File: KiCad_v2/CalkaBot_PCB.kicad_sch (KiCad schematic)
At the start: 38 parts, among them J1 Conn_01x03_Pin, J2 Conn_01x03_Pin, J3 Conn_01x03_Pin, J4 Conn_01x02_Pin, J5 MOTOR3, J6 StartModule, M1 Motor_Right, M2 Motor_Left, Q1 KTIR0711S, Q2 KTIR0711S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

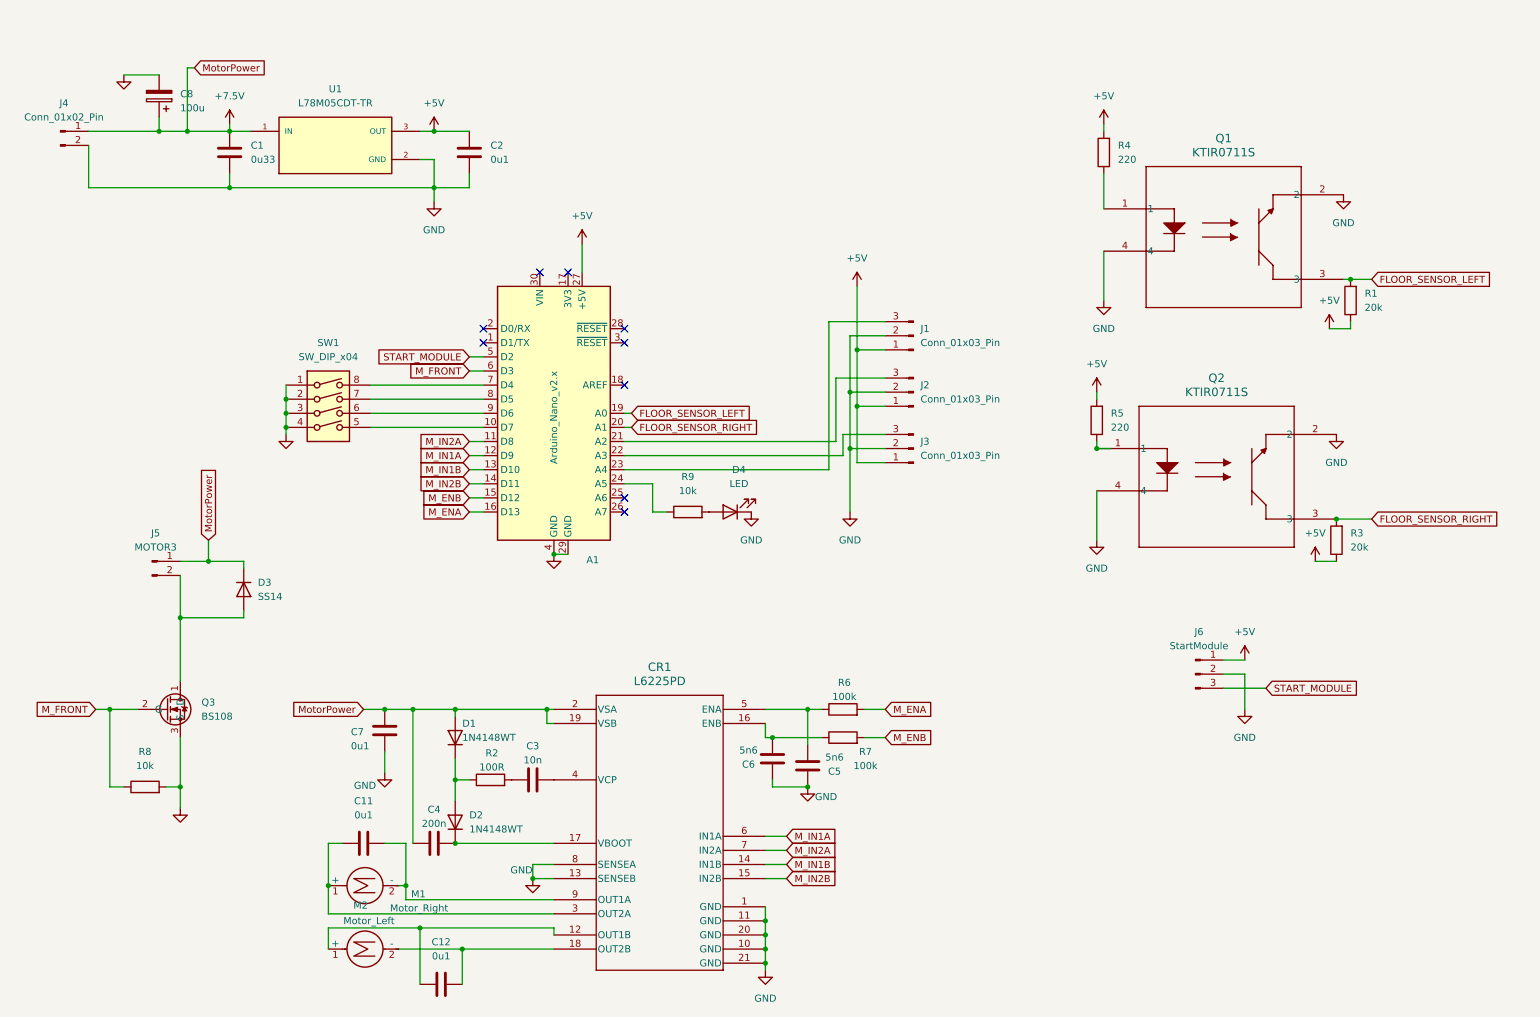
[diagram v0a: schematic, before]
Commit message: Druga płytka działa i jeździ
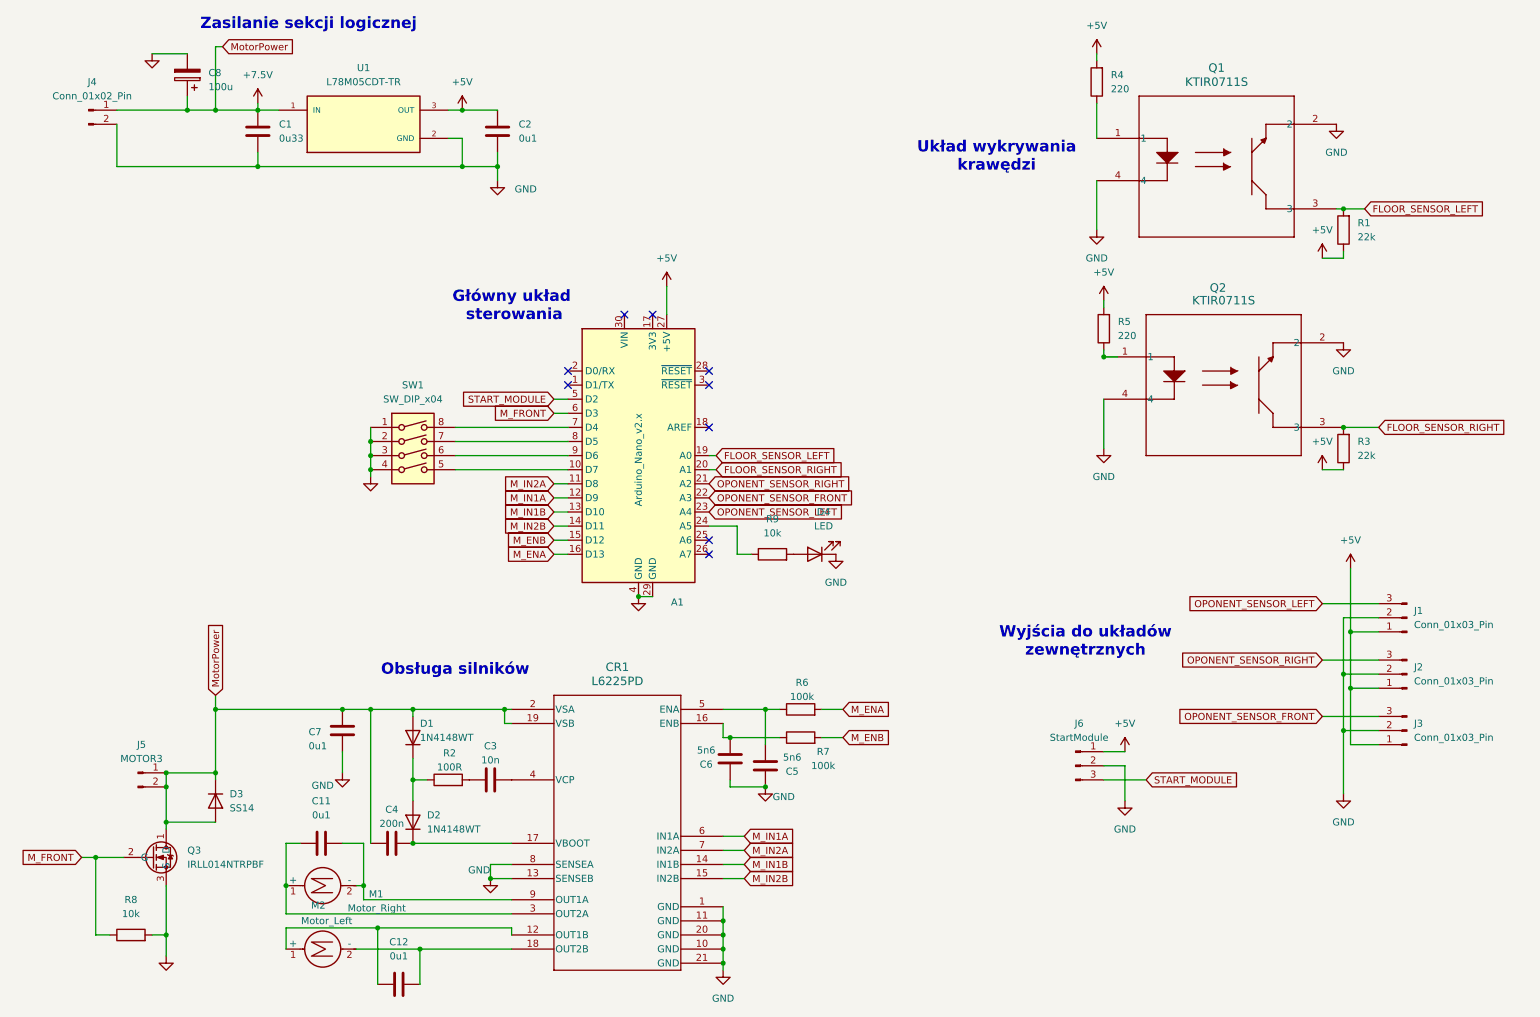
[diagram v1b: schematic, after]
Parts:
- Q3: value BS108 -> IRLL014NTRPBF
- R1, R3: value 20k -> 22k
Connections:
- net +7.5V: now also D3.2 (A), J5.2 (Pin_2), Q3.1 (D)
- net OPONENT_SENSOR_LEFT: now reaches A1.23 (A4), J1.3 (Pin_3)
- net OPONENT_SENSOR_RIGHT: now reaches A1.21 (A2), J2.3 (Pin_3)
- net OPONENT_SENSOR_FRONT: now reaches A1.22 (A3), J3.3 (Pin_3)
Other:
- note added: "Główny układ sterowania"
- note added: "Obsługa silników"
- note added: "Układ wykrywania krawędzi"
- note added: "Wyjścia do układów zewnętrznych"
- note added: "Zasilanie sekcji logicznej"
- company: (none) -> Politechnika Warszawska
- title: (none) -> Minisumo Robot PCB
- moved on the sheet: A1, C1, C11, C12, C2, C3, C4, C5, C6, C7, C8, CR1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
